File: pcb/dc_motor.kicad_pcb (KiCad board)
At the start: 2 copper layers, 76 x 70 mm, 62 parts, among them J1 Conn_01x02, J2 Conn_01x04, J3 Conn_01x04, J4 Conn_01x07, Q1 IPD90P03P4L04, Q2 BTN8982TA, Q3 BTN8982TA, U1 L7805, U2 INA226, U3 74AHC244

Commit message: Diego reviews 1
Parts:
- moved R2 1.75 mm to (103.6, 99.4)
- moved C12 1.37 mm to (70.0, 89.6), turned to 180 degrees
- moved J3 1.31 mm to (95.2, 105.8)
- moved R1 1.12 mm to (101.3, 99.4)
- moved R10 0.98 mm to (94.6, 99.4)
- moved R3 0.57 mm to (99.1, 99.4)
- moved R9 0.47 mm to (96.8, 99.4)
- moved JP1 0.41 mm to (96.2, 91.7)
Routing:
- net GND: track 60.4 -> 52.0 mm, vias 148 -> 150
- net /INH-A: track 16.4 -> 19.2 mm
- net /PWM2: track 27.3 -> 25.8 mm
- net Net-(C10-Pad2): track 28.0 -> 29.3 mm
- net /IN-A: track 15.2 -> 16.4 mm
- net /ALERT: track 14.5 -> 13.4 mm, vias 1 -> 0
- net /IS-A: track 72.3 -> 73.5 mm
- net /A0: track 16.8 -> 15.9 mm
- net /EN_1: track 47.8 -> 46.9 mm
- net /EN_2: track 17.3 -> 16.6 mm
- net +5V: track 77.1 -> 77.7 mm
- net /SDA: track 13.6 -> 13.2 mm, vias 1 -> 0
- net /SCL: track 13.9 -> 14.3 mm, vias 1 -> 0
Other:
- net class integrate added: clearance 0.2, trace_width 0.3, via_dia 0.8, via_drill 0.4
- board text added: "04/11/2020"
- board text added: "5V"
- board text added: "A0"
- board text added: "A1"
- board text added: "Enable"
- board text added: "I2C address"
- board text added: "IND ARG"
- board text added: "Individual"
- board text added: "Luchao90"
- board text added: "Paralell"
- board text added: "Reference specs: MAYER pcb"
- board text added: "Surface finish: HASL with lead"
- board text added: "Tented Vias"
- board text added: "Via Drill: 0.4mm"
- board text added: "Via size: 0.8mm"
- board text removed: "01/12/2020"
- board text removed: "Via Drill: 0.2mm"
- board text removed: "Via size: 0.3mm"

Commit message: add open hardware logo
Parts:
- added LOGO1: Logo_Open_Hardware_Small, Symbol:OSHW-Logo2_9.8x8mm_SilkScreen, F.Cu at (118.0, 64.5)

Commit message: add outputs fab
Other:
- board text added: "Board dimension: 70x76 mm"
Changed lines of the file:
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@@
   (general
     (thickness 1.6)
-    (drawings 63)
+    (drawings 64)
     (tracks 600)
     (zones 0)
@@
   (title_block
     (title "DC MOTOR CONTROL")
-    (date 2020-10-16)
+    (date 2020-11-04)
     (rev "Rev: 1.0")
     (company "NOVOTEC ARGENTINA SRL")
@@
     (pad_drill 3.2)
     (pad_to_mask_clearance 0)
-    (aux_axis_origin 58 100)
+    (aux_axis_origin 48 114)
     (grid_origin 58 108)
     (visible_elements FFFFFF7F)
     (pcbplotparams
-      (layerselection 0x010fc_ffffffff)
+      (layerselection 0x011e8_ffffffff)
       (usegerberextensions false)
       (usegerberattributes true)
@@
       (viasonmask false)
       (mode 1)
-      (useauxorigin false)
+      (useauxorigin true)
       (hpglpennumber 1)
       (hpglpenspeed 20)
@@
     (pad 2 thru_hole oval (at 5.08 0) (size 2.08 3.6) (drill 1.4) (layers *.Cu *.Mask)
       (net 7 "Net-(C10-Pad2)"))
-    (pad 1 thru_hole roundrect (at 0 0) (size 2.08 3.6) (drill 1.4) (layers *.Cu *.Mask) (roundrect_rratio 0.1201913461538461)
+    (pad 1 thru_hole roundrect (at 0 0) (size 2.08 3.6) (drill 1.4) (layers *.Cu *.Mask) (roundrect_rratio 0.1201908653846154)
       (net 1 GND))
     (model ${KISYS3DMOD}/Connector_Phoenix_MSTB.3dshapes/PhoenixContact_MSTBVA_2,5_4-G-5,08_1x04_P5.08mm_Vertical.wrl
@@
     (pad 2 thru_hole oval (at 5.08 0) (size 2.08 3.6) (drill 1.4) (layers *.Cu *.Mask)
       (net 1 GND))
-    (pad 1 thru_hole roundrect (at 0 0) (size 2.08 3.6) (drill 1.4) (layers *.Cu *.Mask) (roundrect_rratio 0.1201913461538461)
+    (pad 1 thru_hole roundrect (at 0 0) (size 2.08 3.6) (drill 1.4) (layers *.Cu *.Mask) (roundrect_rratio 0.1201908653846154)
       (net 6 "Net-(C7-Pad1)"))
     (model ${KISYS3DMOD}/Connector_Phoenix_MSTB.3dshapes/PhoenixContact_MSTBVA_2,5_2-G-5,08_1x02_P5.08mm_Vertical.wrl
@@
     )
   )
-  (gr_text "Tented Vias" (at 149.980952 123.6) (layer Dwgs.User)
+  (gr_text "Board dimension: 70x76 mm" (at 159.6 68.7) (layer Dwgs.User)
     (effects (font (size 2 2) (thickness 0.25)))
   )
-  (gr_text "Surface finish: HASL with lead" (at 164.504762 94.125) (layer Dwgs.User)
+  (gr_text "Tented Vias" (at 146.780952 107.455552) (layer Dwgs.User)
+    (effects (font (size 2 2) (thickness 0.25)))
+  )
+  (gr_text "Surface finish: HASL with lead" (at 161.304762 78.388888) (layer Dwgs.User)
     (effects (font (size 2 2) (thickness 0.25)))
   )
@@
     (effects (font (size 1 1) (thickness 0.15)))
   )
-  (gr_text "Reference specs: MAYER pcb" (at 163.12381 84.3) (layer Dwgs.User)
+  (gr_text "Reference specs: MAYER pcb" (at 159.6 112.3) (layer Dwgs.User)
     (effects (font (size 2 2) (thickness 0.25)))
   )
-  (gr_text "2 Layers - thickness: 1.6 mm" (at 164.6 89.2125) (layer Dwgs.User)
+  (gr_text "2 Layers - thickness: 1.6 mm" (at 161.4 73.544444) (layer Dwgs.User)
     (effects (font (size 2 2) (thickness 0.25)))
   )
-  (gr_text "Grid: 0.1mm" (at 150.6 99.0375) (layer Dwgs.User)
+  (gr_text "Grid: 0.1mm" (at 147.4 83.233332) (layer Dwgs.User)
     (effects (font (size 2 2) (thickness 0.25)))
   )
-  (gr_text "Via Drill: 0.4mm" (at 153.742857 118.6875) (layer Dwgs.User)
+  (gr_text "Via Drill: 0.4mm" (at 150.542857 102.611108) (layer Dwgs.User)
     (effects (font (size 2 2) (thickness 0.25)))
   )
-  (gr_text "Via size: 0.8mm" (at 153.552381 113.775) (layer Dwgs.User)
+  (gr_text "Via size: 0.8mm" (at 150.352381 97.766664) (layer Dwgs.User)
     (effects (font (size 2 2) (thickness 0.25)))
   )
-  (gr_text "Track Width: 0.3mm" (at 156.314286 108.8625) (layer Dwgs.User)
+  (gr_text "Track Width: 0.3mm" (at 153.114286 92.92222) (layer Dwgs.User)
     (effects (font (size 2 2) (thickness 0.25)))
   )
@@
   (gr_arc (start 120 110) (end 120 114) (angle -90) (layer Edge.Cuts) (width 0.3))
   (gr_arc (start 52 110) (end 48 110) (angle -90) (layer Edge.Cuts) (width 0.3))
-  (gr_text "Clearance: 0.2 mm" (at 155.790476 103.95) (layer Dwgs.User)
+  (gr_text "Clearance: 0.2 mm" (at 152.590476 88.077776) (layer Dwgs.User)
     (effects (font (size 2 2) (thickness 0.25)))
   )
@@
   )
   (dimension 76 (width 0.15) (layer Dwgs.User)
-    (gr_text "76,000 mm" (at 86 117.4) (layer Dwgs.User)
+    (gr_text "76,000 mm" (at 86 121) (layer Dwgs.User)
       (effects (font (size 1 1) (thickness 0.15)))
     )
-    (feature1 (pts (xy 124 110) (xy 124 116.686421)))
-    (feature2 (pts (xy 48 110) (xy 48 116.686421)))
-    (crossbar (pts (xy 48 116.1) (xy 124 116.1)))
-    (arrow1a (pts (xy 124 116.1) (xy 122.873496 116.686421)))
-    (arrow1b (pts (xy 124 116.1) (xy 122.873496 115.513579)))
-    (arrow2a (pts (xy 48 116.1) (xy 49.126504 116.686421)))
-    (arrow2b (pts (xy 48 116.1) (xy 49.126504 115.513579)))
+    (feature1 (pts (xy 124 110) (xy 124 120.286421)))
+    (feature2 (pts (xy 48 110) (xy 48 120.286421)))
+    (crossbar (pts (xy 48 119.7) (xy 124 119.7)))
+    (arrow1a (pts (xy 124 119.7) (xy 122.873496 120.286421)))
+    (arrow1b (pts (xy 124 119.7) (xy 122.873496 119.113579)))
+    (arrow2a (pts (xy 48 119.7) (xy 49.126504 120.286421)))
+    (arrow2b (pts (xy 48 119.7) (xy 49.126504 119.113579)))
   )
   (gr_line (start 124 48) (end 124 110) (layer Edge.Cuts) (width 0.3))

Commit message: economic BOM
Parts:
- added J5: Conn_01x02, Connector_Phoenix_MC_HighVoltage:PhoenixContact_MCV_1,5_2-G-5.08_1x02_P5.08mm_Vertical, F.Cu at (81.8, 58.0)
- D2: value Green led 0603 -> Red led 0603
- D3: value Yellow led 0603 -> Red led 0603
- D4: value Blue led 0603 -> Red led 0603
- J1: footprint Connector_Phoenix_MSTB:PhoenixContact_MSTBVA_2,5_2-G-5,08_1x02_P5.08mm_Vertical -> Connector_Phoenix_MC_HighVoltage:PhoenixContact_MCV_1,5_2-G-5.08_1x02_P5.08mm_Vertical
- J2: value Conn_01x04 -> Conn_01x02; footprint Connector_Phoenix_MSTB:PhoenixContact_MSTBVA_2,5_4-G-5,08_1x04_P5.08mm_Vertical -> Connector_Phoenix_MC_HighVoltage:PhoenixContact_MCV_1,5_2-G-5.08_1x02_P5.08mm_Vertical
- Q1: value IPD90P03P4L04 -> IPD50P04P4L11
- Q2, Q3: value BTN8982TA -> BTN8962

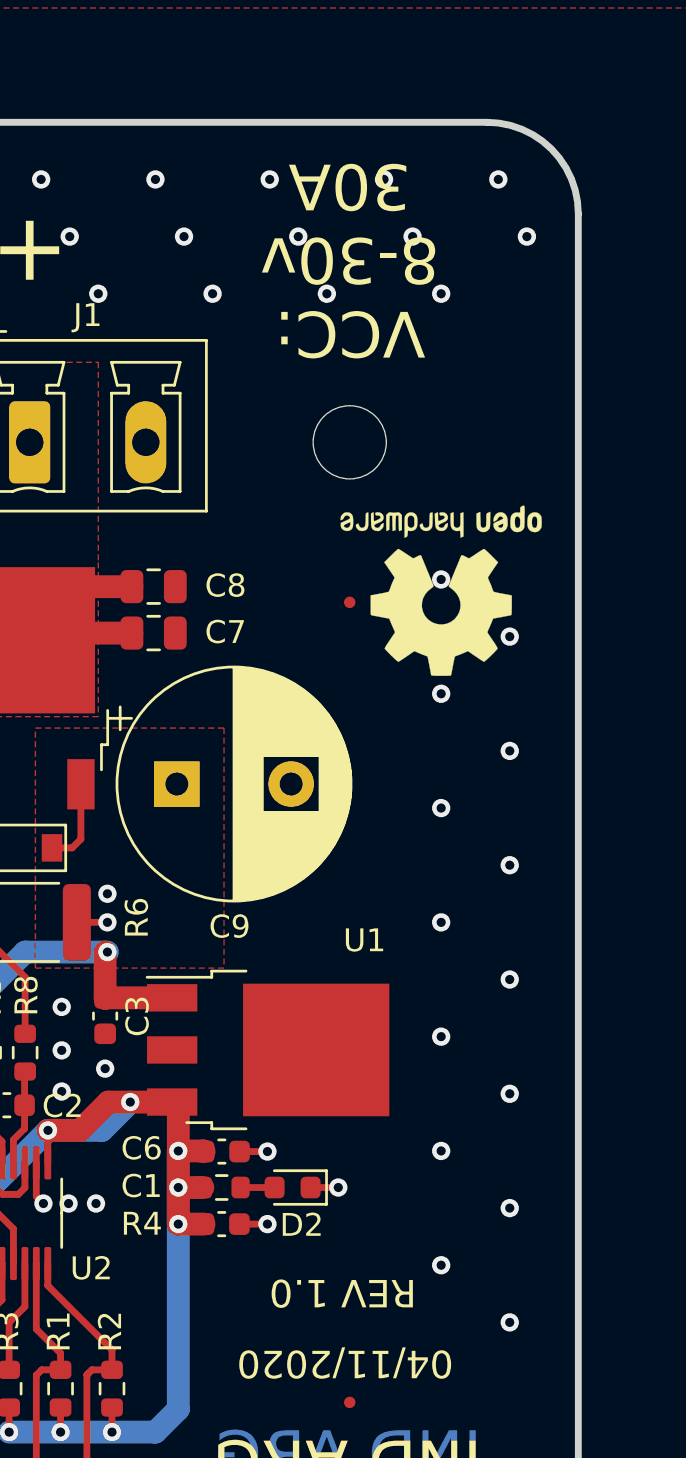
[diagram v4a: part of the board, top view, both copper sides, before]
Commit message: Rev 1.1
Change power connectors and limited current to 20A
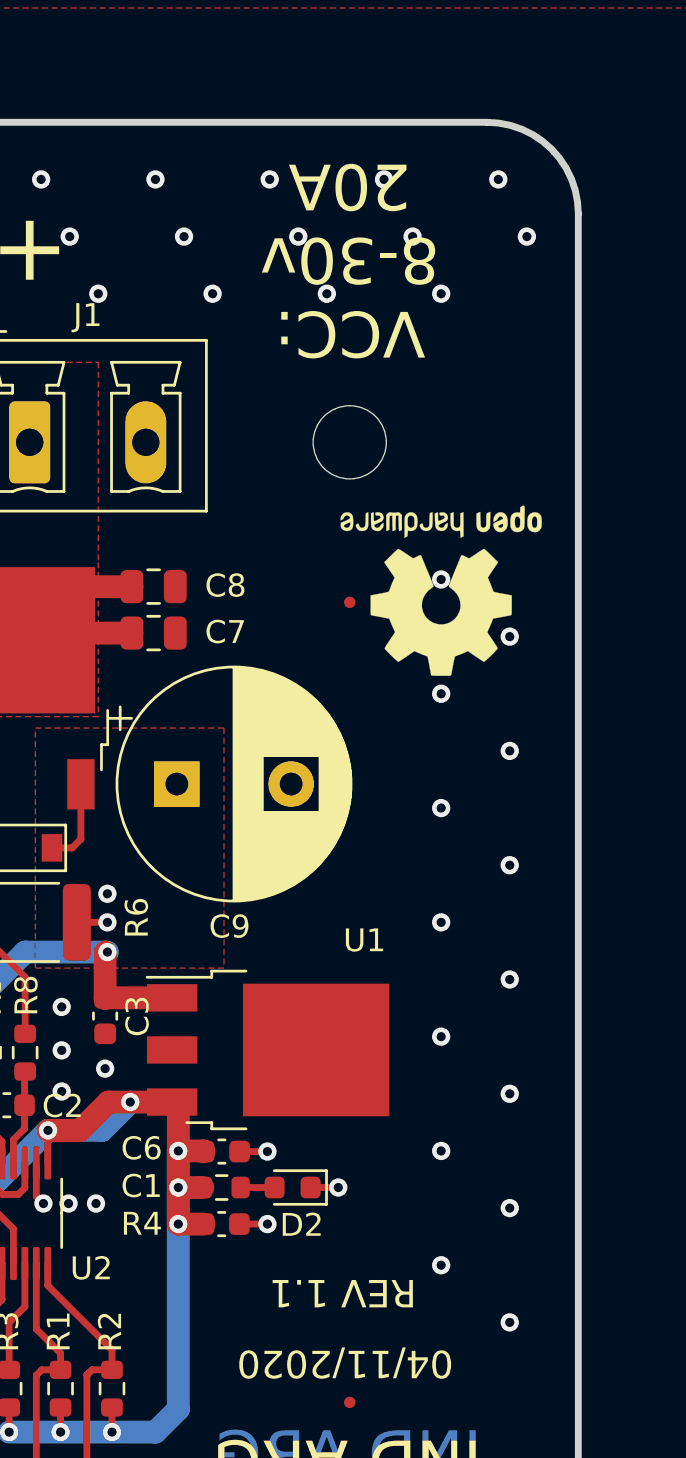
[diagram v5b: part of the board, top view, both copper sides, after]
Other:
- board text added: "REV 1.1"
- board text added: "VCC: 8-30v 20A"
- board text removed: "REV 1.0"
- board text removed: "Reference specs: MAYER pcb"
- board text removed: "VCC: 8-30v 30A"
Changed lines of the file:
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@@
   (general
     (thickness 1.6)
-    (drawings 64)
+    (drawings 63)
     (tracks 600)
     (zones 0)
@@
   (title_block
     (title "DC MOTOR CONTROL")
-    (date 2020-11-04)
-    (rev "Rev: 1.0")
+    (date 2020-11-15)
+    (rev "Rev: 1.1")
     (company "NOVOTEC ARGENTINA SRL")
     (comment 1 "Author: Ing. Luciano Vittori")
@@
     )
   )
+  (gr_text lucianovittori99@gmail.com (at 52.6 75.4 90) (layer F.SilkS)
+    (effects (font (size 2 2) (thickness 0.4)))
+  )
   (gr_text "Board dimension: 70x76 mm" (at 159.6 68.7) (layer Dwgs.User)
     (effects (font (size 2 2) (thickness 0.25)))
@@
     (effects (font (size 1 1) (thickness 0.15)))
   )
-  (gr_text "Reference specs: MAYER pcb" (at 159.6 112.3) (layer Dwgs.User)
-    (effects (font (size 2 2) (thickness 0.25)))
-  )
   (gr_text "2 Layers - thickness: 1.6 mm" (at 161.4 73.544444) (layer Dwgs.User)
     (effects (font (size 2 2) (thickness 0.25)))
@@
     (effects (font (size 2 2) (thickness 0.25)))
   )
-  (gr_text lucianovittori99@gmail.com (at 52.6 75.4 90) (layer F.SilkS)
-    (effects (font (size 2 2) (thickness 0.4)))
-  )
   (gr_text "github: Luchao90" (at 56.9 74.5 90) (layer F.SilkS)
     (effects (font (size 2 2) (thickness 0.4)))
   )
-  (gr_text "REV 1.0" (at 113.7 95.2 180) (layer F.SilkS)
+  (gr_text "REV 1.1" (at 113.7 95.2 180) (layer F.SilkS)
     (effects (font (size 1.2 1.2) (thickness 0.3)))
   )
@@
     (effects (font (size 1.5 1.5) (thickness 0.3)))
   )
-  (gr_text "VCC:\n8-30v\n30A" (at 114 50 180) (layer F.SilkS)
+  (gr_text "VCC:\n8-30v\n20A" (at 114 50 180) (layer F.SilkS)
     (effects (font (size 2 2) (thickness 0.35)))
   )
